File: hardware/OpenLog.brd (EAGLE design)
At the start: 17.8 x 19.1 mm, 19 parts, among them Q1 16MHZ, U1 ATMEGA328P_TQFP, U2 3.3V MIC5205, U3 microSD Socket

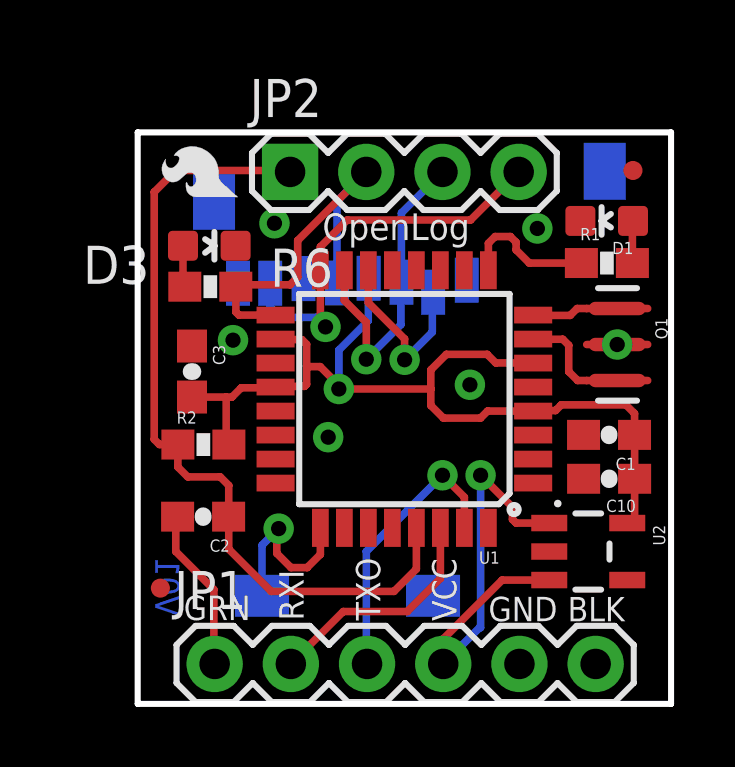
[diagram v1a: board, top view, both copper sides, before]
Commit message: Added OSHW Logo
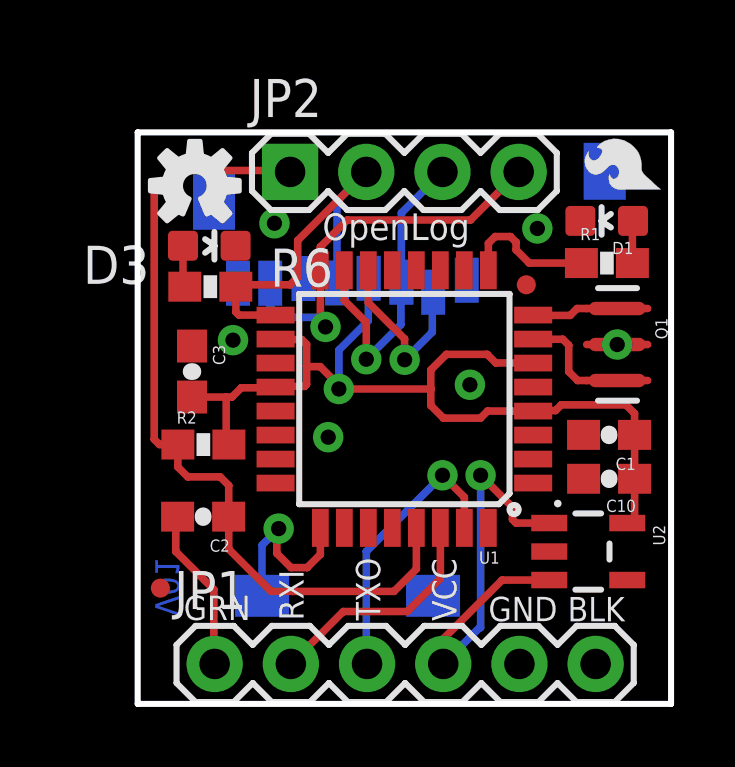
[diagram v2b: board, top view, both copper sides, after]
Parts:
- added LOGO2: OSHW-LOGOS, SparkFun-Aesthetics:OSHW-LOGO-S
- moved LOGO1 14.1 mm to (36.8, 6.67)
- moved FID1 5.21 mm to (32.0, 3.81)
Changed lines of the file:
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@@
 <layer number="27" name="tValues" color="7" fill="1" visible="no" active="yes"/>
 <layer number="28" name="bValues" color="7" fill="1" visible="no" active="yes"/>
-<layer number="29" name="tStop" color="7" fill="3" visible="no" active="yes"/>
+<layer number="29" name="tStop" color="7" fill="3" visible="yes" active="yes"/>
 <layer number="30" name="bStop" color="7" fill="6" visible="no" active="yes"/>
 <layer number="31" name="tCream" color="7" fill="4" visible="no" active="yes"/>
@@
 <attribute name="DESIGNER" value="NAME" x="-2.012121875" y="-19.05" size="1.778" layer="27" display="off"/>
 </element>
-<element name="LOGO1" library="SparkFun-Aesthetics" package="SFE_LOGO_FLAME_.1" value="SFE_LOGO_FLAME.1_INCH" x="22.7482375" y="6.413496875" rot="R90"/>
-<element name="FID1" library="SparkFun-Aesthetics" package="MICRO-FIDUCIAL" value="FIDUCIALUFIDUCIAL" x="35.56" y="7.62"/>
+<element name="LOGO1" library="SparkFun-Aesthetics" package="SFE_LOGO_FLAME_.1" value="SFE_LOGO_FLAME.1_INCH" x="36.8452375" y="6.667496875" rot="R90"/>
+<element name="FID1" library="SparkFun-Aesthetics" package="MICRO-FIDUCIAL" value="FIDUCIALUFIDUCIAL" x="32.004" y="3.81"/>
 <element name="FID2" library="SparkFun-Aesthetics" package="MICRO-FIDUCIAL" value="FIDUCIALUFIDUCIAL" x="19.80691875" y="-6.301740625"/>
+<element name="LOGO2" library="SparkFun-Aesthetics" package="OSHW-LOGO-S" value="OSHW-LOGOS" x="20.955" y="7.112"/>
 </elements>
 <signals>

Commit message: Fixed Version #
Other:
- board text added: "V12"
- board text removed: "V01"
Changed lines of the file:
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@@
 <layer number="27" name="tValues" color="7" fill="1" visible="no" active="yes"/>
 <layer number="28" name="bValues" color="7" fill="1" visible="no" active="yes"/>
-<layer number="29" name="tStop" color="7" fill="3" visible="yes" active="yes"/>
+<layer number="29" name="tStop" color="7" fill="3" visible="no" active="yes"/>
 <layer number="30" name="bStop" color="7" fill="6" visible="no" active="yes"/>
 <layer number="31" name="tCream" color="7" fill="4" visible="no" active="yes"/>
@@
 <text x="28.366721875" y="-19.177" size="1.778" layer="51" font="vector" ratio="10">N. Seidle</text>
 <text x="9.53261875" y="-21.73731875" size="1.778" layer="51" font="vector" ratio="10">Revised by: Patrick Alberts</text>
-<text x="20.444459375" y="-5.27558125" size="0.8128" layer="16" font="vector" ratio="12" rot="MR270">V01</text>
+<text x="20.444459375" y="-5.27558125" size="0.8128" layer="16" font="vector" ratio="12" rot="MR270">V12</text>
 </plain>
 <attributes>

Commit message: Fixed  QC issues
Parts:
- moved FRAME1 6.48 mm to (-0.74, -25.4)
- moved LOGO1 0.31 mm to (36.5, 6.63)
- moved D1 0.22 mm to (34.9, 5.94)
- moved R1 0.22 mm to (34.9, 4.53)
- moved R6 0.12 mm to (21.4, 3.76)
- moved D3 0.12 mm to (21.3, 5.12)
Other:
- board text added: "0.8mm Thin PCB"
- board text added: "DI"
- board text added: "DO"
- board text added: "RST"
- board text added: "SCK"
